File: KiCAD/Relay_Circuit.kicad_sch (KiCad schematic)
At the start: 6 parts, among them K1 G5V-1, U2 PC12311NSZ1B

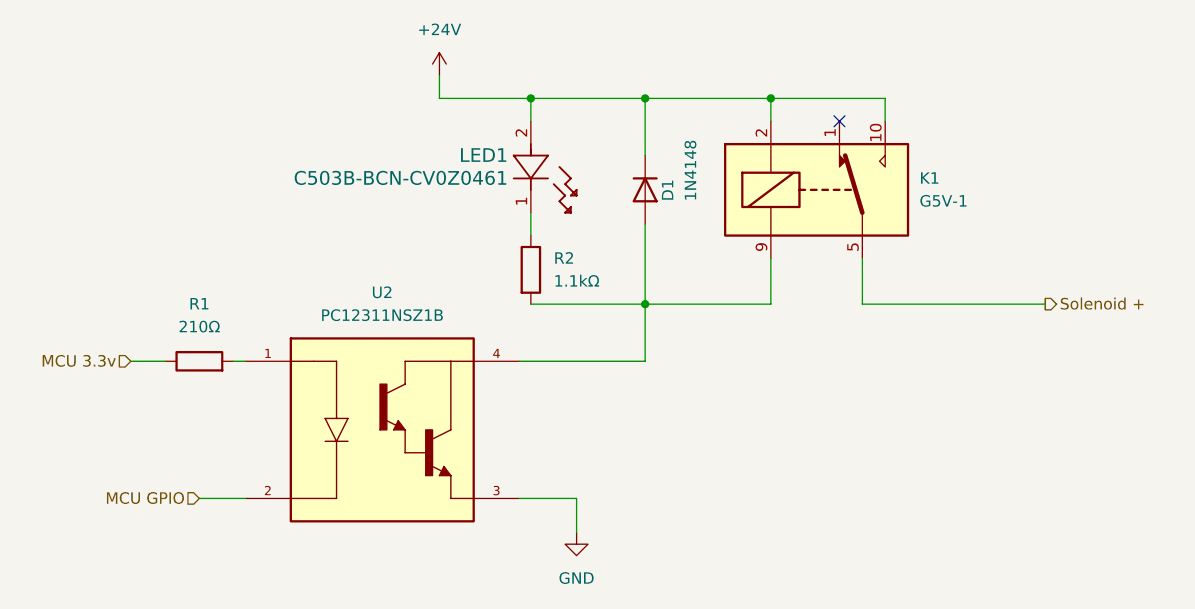
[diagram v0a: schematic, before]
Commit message: Fixed Silkscreen Labels for Components
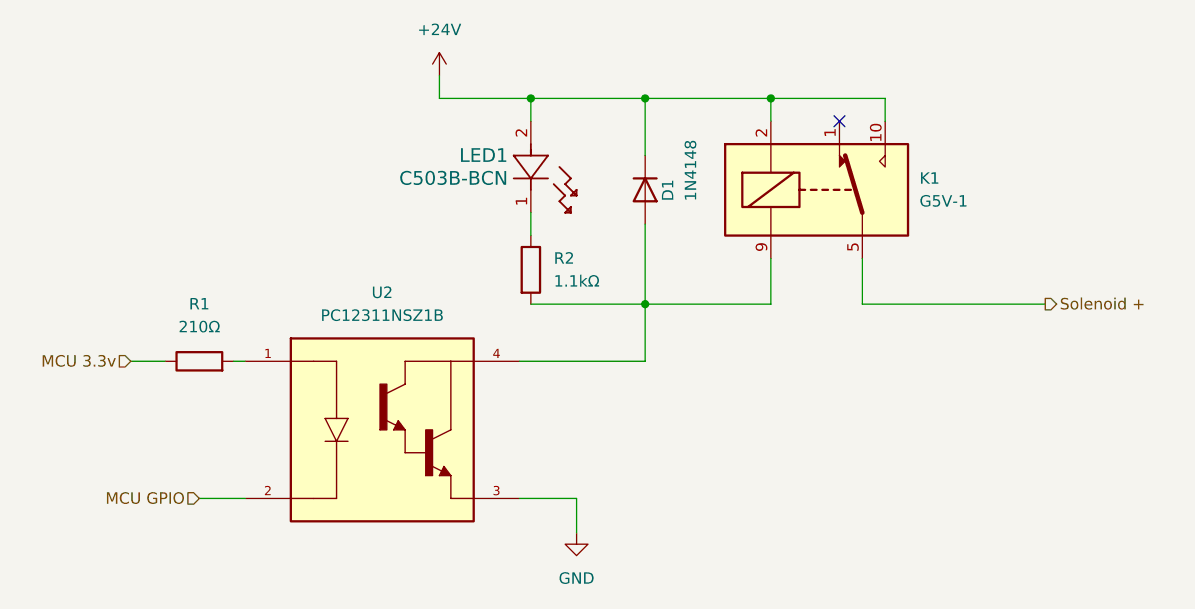
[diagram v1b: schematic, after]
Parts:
- D1: footprint Diode_THT:D_DO-35_SOD27_P7.62mm_Horizontal -> Diode_THT:D_DO-35_SOD27_P7.62mm_Horizontal-JW
- LED1: value C503B-BCN-CV0Z0461 -> C503B-BCN
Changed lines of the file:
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@@
       (effects (font (size 1.524 1.524)) (justify right))
     )
-    (property "Value" "C503B-BCN-CV0Z0461" (at 160.02 72.39 90)
+    (property "Value" "C503B-BCN" (at 160.02 72.39 90)
       (effects (font (size 1.524 1.524)) (justify right))
     )
@@
       (effects (font (size 1.27 1.27)) (justify right))
     )
-    (property "Footprint" "Diode_THT:D_DO-35_SOD27_P7.62mm_Horizontal" (at 175.26 73.66 0)
+    (property "Footprint" "Diode_THT:D_DO-35_SOD27_P7.62mm_Horizontal-JW" (at 175.26 73.66 0)
       (effects (font (size 1.27 1.27)) hide)
     )
